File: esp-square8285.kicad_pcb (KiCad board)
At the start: 2 copper layers, 21.3 x 26.4 mm, 17 parts

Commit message: Jan 2017
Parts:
- removed the ? at (150.6, 49.8)
- removed the ? at (144.5, 62.0)
- removed OLED: SSD1306, oled:SSD1306
- removed RGBLED: 3535, ws2812:3535
- added 3535: 3535, ws2812:3535, F.Cu at (149.1, 55.9)
- added ?: C_0603, Capacitors_SMD:C_0603, F.Cu at (151.3, 45.1)
- added ?: C_0603, Capacitors_SMD:C_0603, F.Cu at (150.8, 50.3)
- added ?: R_0603, Resistors_SMD:R_0603, F.Cu at (144.4, 60.0)
- added Crystal: Crystal_SMD_2016_4Pads, Crystals:Crystal_SMD_2016_4Pads, F.Cu at (150.6, 47.5)
- added REF**: Pin_Header_Straight_2x01, Pin_Headers:Pin_Header_Straight_2x01, F.Cu at (147.8, 52.8)
- added SERIAL: Pin 1x03, Pin_Headers:Pin_Header_Straight_1x03, F.Cu at (141.2, 62.2)
- moved GPIO0 1.10 mm to (137.9, 59.4)
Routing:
- net (no net): track 332.6 -> 359.5 mm, vias 33 -> 35
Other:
- board text added: "donp.org 2017 Jan"
- board text removed: "donp.org 2016 Nov"

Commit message: 2017 Feb
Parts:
- added ?: R_0603, Resistors_SMD:R_0603, F.Cu at (133.7, 49.7)
- moved ? 0.70 mm to (133.7, 46.2)
- moved ? 0.40 mm to (133.7, 40.8)
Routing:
- net (no net): track 359.5 -> 374.9 mm, vias 35 -> 38
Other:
- board text added: "donp.org 2017 Feb"
- board text removed: "donp.org 2017 Jan"

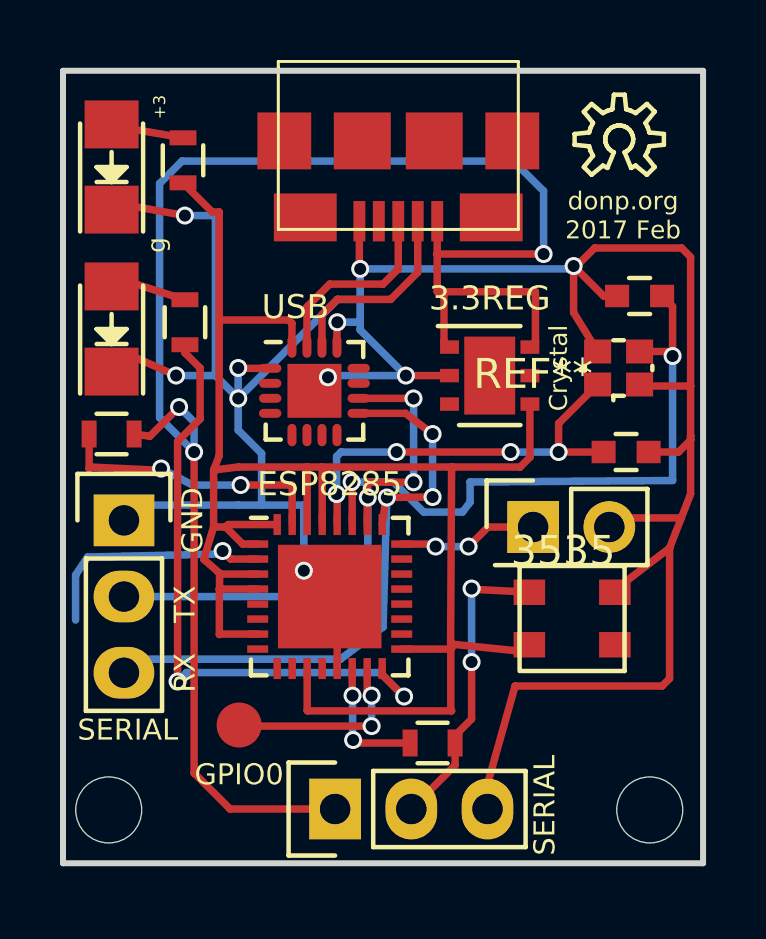
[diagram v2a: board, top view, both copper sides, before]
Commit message: bump down 3535
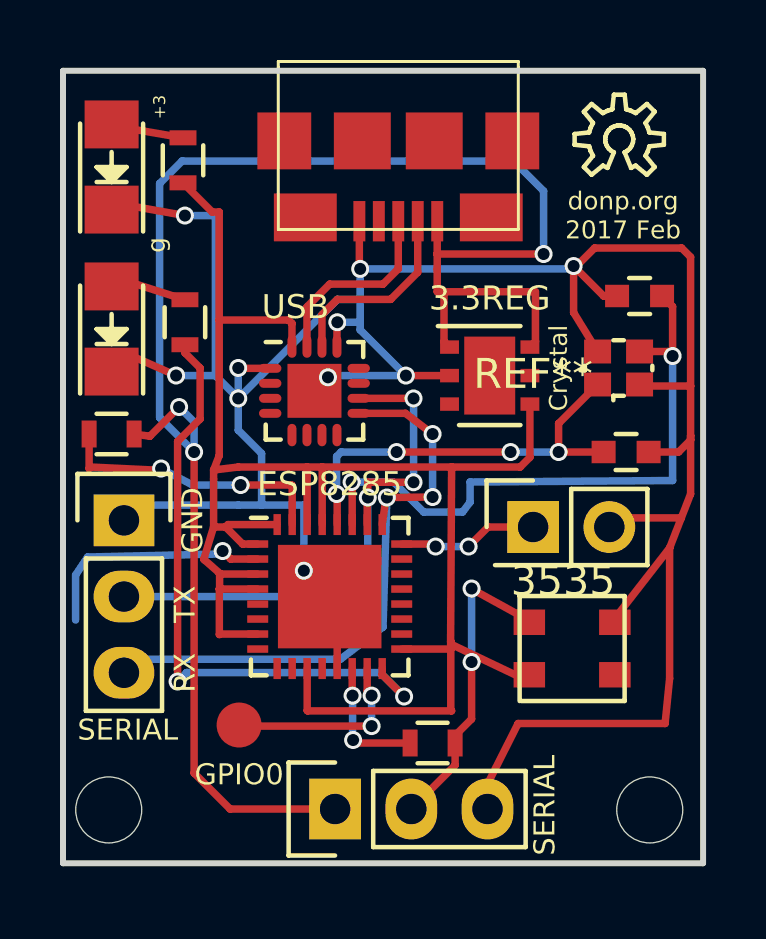
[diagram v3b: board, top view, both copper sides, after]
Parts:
- moved 3535 1.00 mm to (149.1, 56.9)
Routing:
- net (no net): track 374.9 -> 376.2 mm
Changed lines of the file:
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@@
   )
   (module ws2812:3535 (layer F.Cu)
-    (at 149.05 55.85 180)
+    (at 149.05 56.85 180)
     (fp_text reference 3535 (at 0.3 2.25 180) (layer F.SilkS)
       (effects (font (size 1 1) (thickness 0.15)))
@@
     (effects (font (size 0.6 0.6) (thickness 0.1)))
   )
-  (segment (start 132.95 49.7) (end 132.95 50.85) (width 0.25) (layer F.Cu) (net 0) (status 400000))
-  (segment (start 139.72 51.42) (end 139.72 52.718) (width 0.25) (layer F.Cu) (net 0) (status 800000))
+  (segment (start 132.95 49.7) (end 132.95 50.85) (width 0.25) (layer F.Cu) (net 0))
+  (segment (start 139.72 51.42) (end 139.72 52.718) (width 0.25) (layer F.Cu) (net 0))
   (segment (start 139.7 51.4) (end 139.72 51.42) (width 0.25) (layer F.Cu) (net 0))
   (segment (start 138 51.4) (end 139.7 51.4) (width 0.25) (layer F.Cu) (net 0))
@@
   (segment (start 145.15 60) (end 145.15 59.75) (width 0.25) (layer F.Cu) (net 0))
   (segment (start 145.15 59.75) (end 145.7 59.2) (width 0.25) (layer F.Cu) (net 0))
-  (segment (start 145.725 54.875) (end 147.725 54.975) (width 0.25) (layer F.Cu) (net 0) (status 20))
+  (segment (start 145.725 54.875) (end 147.725 55.975) (width 0.25) (layer F.Cu) (net 0) (status 20))
   (segment (start 145.7 54.85) (end 145.725 54.875) (width 0.25) (layer F.Cu) (net 0))
   (via (at 145.7 54.85) (size 0.6) (drill 0.4) (layers F.Cu B.Cu) (net 0))
@@
   (segment (start 145.15 60.74) (end 143.69 62.2) (width 0.25) (layer F.Cu) (net 0))
   (segment (start 146.23 62.2) (end 146.23 61.37) (width 0.25) (layer F.Cu) (net 0) (status 30))
-  (segment (start 146.23 61.37) (end 147.15 58.1) (width 0.25) (layer F.Cu) (net 0) (status 10))
-  (segment (start 147.15 58.1) (end 152.05 58.1) (width 0.25) (layer F.Cu) (net 0))
-  (segment (start 152.05 58.1) (end 152.3 57.85) (width 0.25) (layer F.Cu) (net 0))
+  (segment (start 146.23 61.37) (end 147.25 59.35) (width 0.25) (layer F.Cu) (net 0) (status 10))
+  (segment (start 147.25 59.35) (end 152.15 59.35) (width 0.25) (layer F.Cu) (net 0))
+  (segment (start 152.15 59.35) (end 152.3 57.85) (width 0.25) (layer F.Cu) (net 0))
   (segment (start 152.3 57.85) (end 152.3 53.5) (width 0.25) (layer F.Cu) (net 0))
   (segment (start 143.7 62.19) (end 143.69 62.2) (width 0.25) (layer F.Cu) (net 0) (status 30))
@@
   (via (at 141.75 59.9) (size 0.6) (drill 0.4) (layers F.Cu B.Cu) (net 0))
   (segment (start 141.732 59.882) (end 141.75 59.9) (width 0.25) (layer B.Cu) (net 0))
-  (segment (start 147.675 56.975) (end 145 56.7) (width 0.25) (layer F.Cu) (net 0) (status 10))
+  (segment (start 147.675 57.975) (end 145 56.7) (width 0.25) (layer F.Cu) (net 0) (status 10))
   (segment (start 145.016 56.625) (end 145 56.625) (width 0.25) (layer F.Cu) (net 0))
   (segment (start 145.016 56.684) (end 145.016 56.625) (width 0.25) (layer F.Cu) (net 0))
@@
   (segment (start 153 51.7) (end 152.690349 52.496245) (width 0.25) (layer F.Cu) (net 0))
   (segment (start 152.690349 52.496245) (end 152.3 53.5) (width 0.25) (layer F.Cu) (net 0))
-  (segment (start 152.3 53.5) (end 150.375 54.975) (width 0.25) (layer F.Cu) (net 0) (status 20))
+  (segment (start 152.3 53.5) (end 150.375 55.975) (width 0.25) (layer F.Cu) (net 0) (status 20))
   (segment (start 148.6 50.3) (end 148.6 49.35) (width 0.25) (layer F.Cu) (net 0))
   (segment (start 148.6 49.35) (end 149.9 48.05) (width 0.25) (layer F.Cu) (net 0))

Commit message: start over 8285
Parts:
- removed the ? at (144.4, 60.0)
- removed the ? at (133.7, 46.2)
- removed the ? at (136.1, 46.0)
- removed the ? at (133.6, 62.2)
- removed GPIO0: Measure, Measurement_Points:Measurement_Point_Round-SMD-Pad_Small
- removed REF**: Pin_Header_Straight_2x01, Pin_Headers:Pin_Header_Straight_2x01
- moved R12 17.3 mm to (150.8, 52.0)
- moved ? 16.4 mm to (135.0, 45.8)
- moved ? 16.3 mm to (135.1, 44.0)
- moved Crystal 15.8 mm to (134.8, 48.8)
- moved USB 7.94 mm to (148.3, 47.2)
- moved 3.3REG 5.74 mm to (140.7, 46.8)
- moved serial 4.32 mm to (134.1, 56.9)
- moved ESP8285 2.03 mm to (143.0, 55.1)
- moved ? 1.92 mm to (135.2, 39.6), turned to 0 degrees
- moved neopix 1.69 mm to (150.7, 56.3), turned to 0 degrees
- moved ? 1.52 mm to (136.4, 42.0), turned to 0 degrees
- gave numbers to parts that had none: 1
- renumbered 3535 to neopix, SERIAL to pixport, SERIAL to serial
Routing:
- net (no net): track 376.2 -> 0.00 mm, vias 38 -> 0
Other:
- board text added: "donp.org 2017 Mar"
- board text removed: "donp.org 2017 Feb"
- board text removed: "g"
